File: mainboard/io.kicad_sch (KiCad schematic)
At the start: 72 parts, among them J10 LASER-, J11 MTR+, J13 MTR-, J5 Micro_SD_Card, J6 TT143AMC12C, J9 LASER+, Q1 BSS214NW, SW2 B3U-3000P-B, SW3 B3U-3000P-B, SW4 B3U-3000P-B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

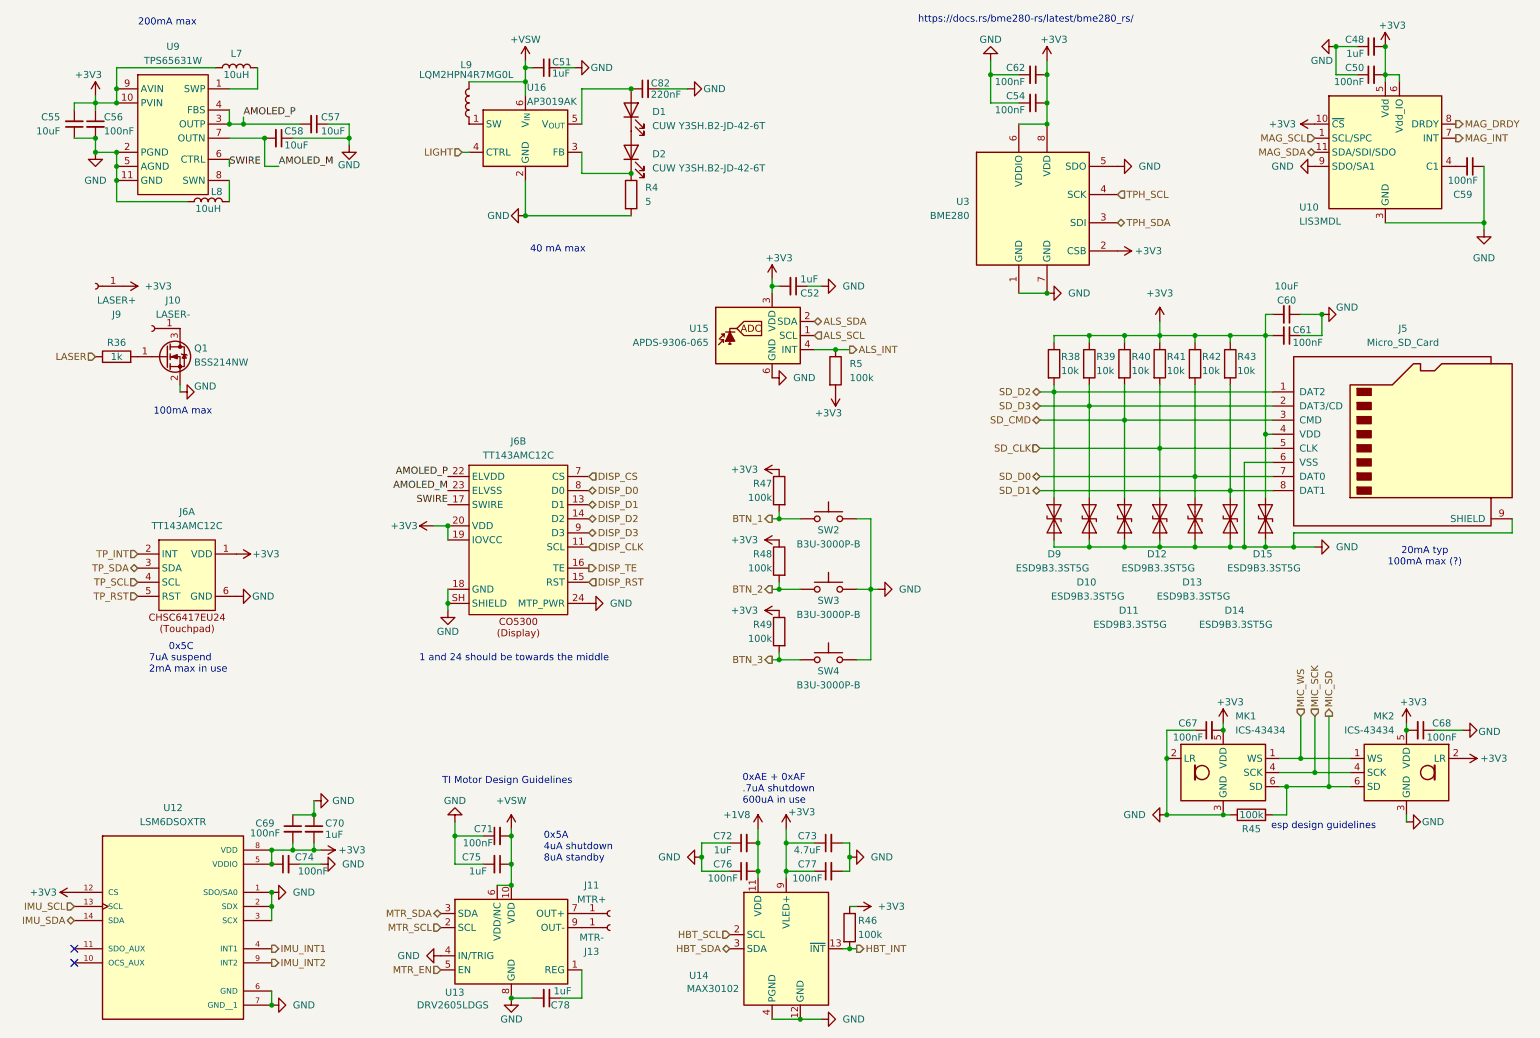
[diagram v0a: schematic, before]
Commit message: remove all features idrc abt from schematic
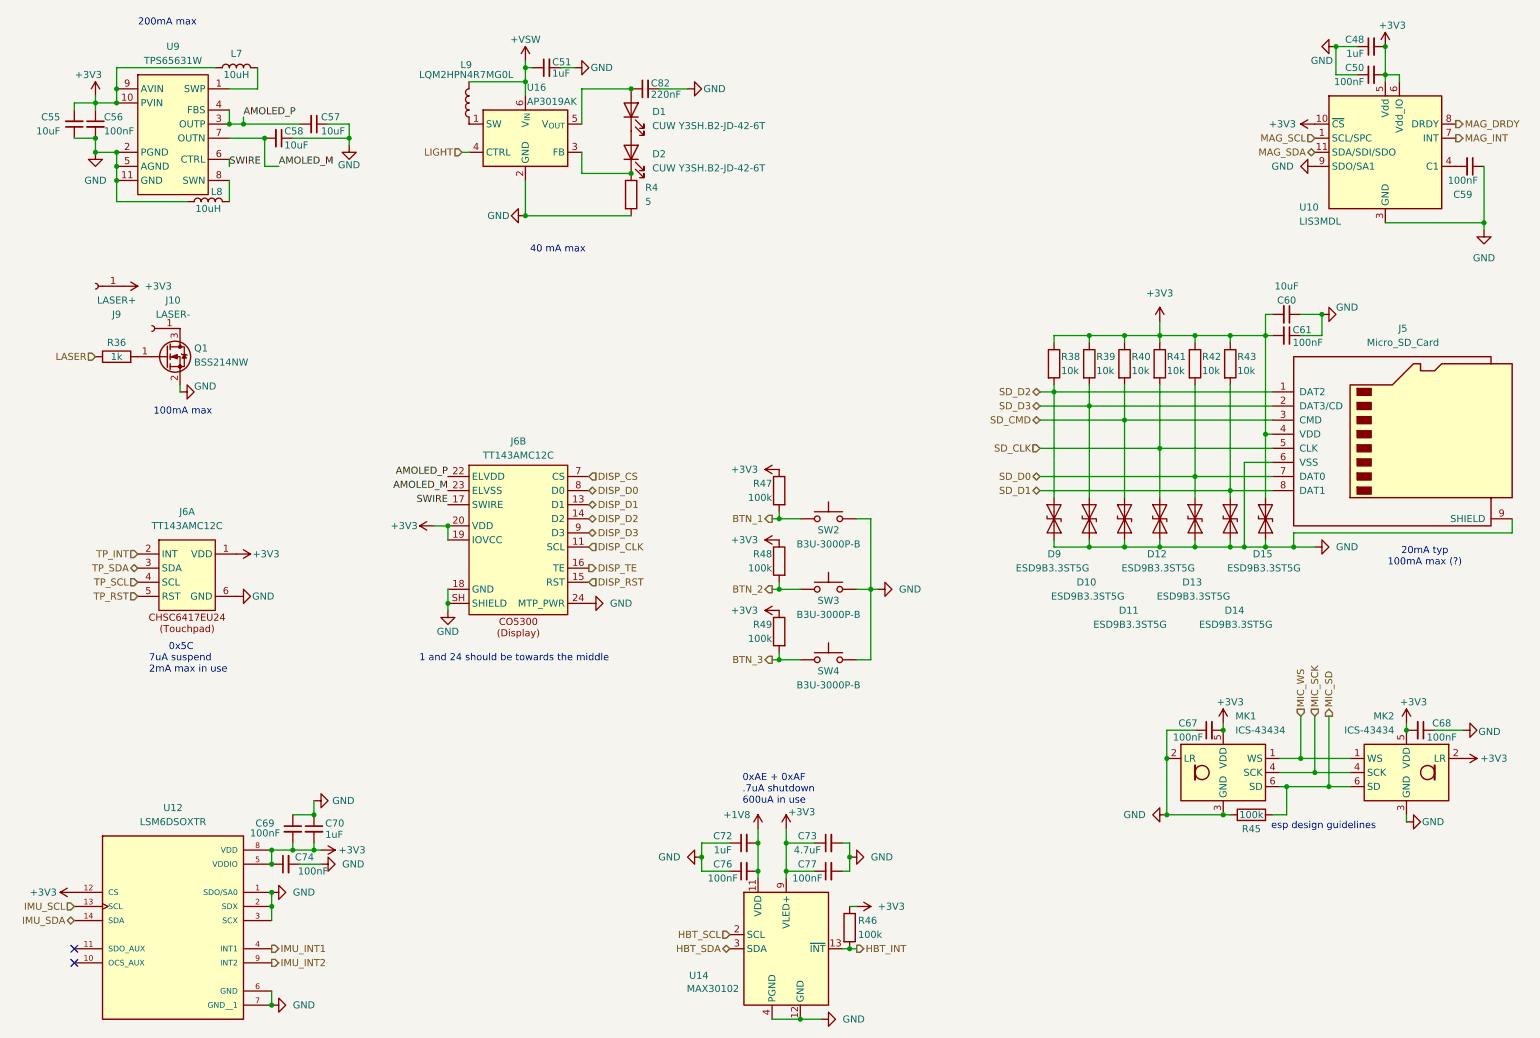
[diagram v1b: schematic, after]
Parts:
- removed C52, C75, C78: 1uF, Capacitor_SMD:C_0402_1005Metric, symbol Device:C_Small
- removed C54, C62, C71: 100nF, Capacitor_SMD:C_0402_1005Metric, symbol Device:C_Small
- removed J11: MTR+, TestPoint:TestPoint_THTPad_1.5x1.5mm_Drill0.7mm, symbol Connector:Conn_01x01_Socket
- removed J13: MTR-, TestPoint:TestPoint_THTPad_1.5x1.5mm_Drill0.7mm, symbol Connector:Conn_01x01_Socket
- removed R5: 100k, Resistor_SMD:R_0402_1005Metric, symbol Device:R
- removed U13: DRV2605LDGS, Package_SO:VSSOP-10_3x3mm_P0.5mm, symbol Driver_Haptic:DRV2605LDGS
- removed U15: APDS-9306-065, OptoDevice:Broadcom_DFN-6_2x2mm_P0.65mm, symbol Sensor_Optical:APDS-9306-065
- removed U3: BME280, Package_LGA:Bosch_LGA-8_2.5x2.5mm_P0.65mm_ClockwisePinNumbering, symbol Sensor:BME280
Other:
- note removed: "0x5A 4uA shutdown 8uA standby"
- note removed: "TI Motor Design Guidelines"
- note removed: "https://docs.rs/bme280-rs/latest/bme280_rs/"
